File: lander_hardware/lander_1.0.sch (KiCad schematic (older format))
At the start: 26 parts, among them IC1 ATMEGA328-P, J1 Power Connector, P1 Power Supplement, P2 ICSP, P3 XBEE Out, P4 Digital Supplement 1, P5 Digital Supplement 2, P6 Analog Supplement, U1 LD1117S33TR, U2 7805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

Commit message: Simplified continuity tester
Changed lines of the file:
@@
 $EndSheet
 $Comp
-L GND #PWR23
+L GND #PWR22
 U 1 1 58B64C68
 P 11000 3400
-F 0 "#PWR23" H 11000 3150 50  0001 C CNN
+F 0 "#PWR22" H 11000 3150 50  0001 C CNN
 F 1 "GND" H 11000 3250 50  0000 C CNN
 F 2 "" H 11000 3400 50  0000 C CNN
@@
 $EndComp
 $Comp
-L +3.3V #PWR22
+L +3.3V #PWR21
 U 1 1 58B64CE8
 P 11000 2500
-F 0 "#PWR22" H 11000 2350 50  0001 C CNN
+F 0 "#PWR21" H 11000 2350 50  0001 C CNN
 F 1 "+3.3V" H 11000 2640 50  0000 C CNN
 F 2 "" H 11000 2500 50  0000 C CNN
@@
 F6 "Pyro2" I L 9100 4950 60
 F7 "Pyro3" I L 9100 5050 60
-F8 "3.3Vin" I R 10200 4550 60
-F9 "6Vin" I R 10200 4650 60
-F10 "GNDin" I R 10200 4750 60
+F8 "6Vin" I R 10200 4650 60
+F9 "GNDin" I R 10200 4750 60
 $EndSheet
 $Comp
-L +3.3V #PWR19
-U 1 1 58B72CA4
-P 10400 4550
-F 0 "#PWR19" H 10400 4400 50  0001 C CNN
-F 1 "+3.3V" H 10400 4690 50  0000 C CNN
-F 2 "" H 10400 4550 50  0000 C CNN
-F 3 "" H 10400 4550 50  0000 C CNN
-	1    10400 4550
-	1    0    0    -1
-$EndComp
-$Comp
-L +6V #PWR21
+L +6V #PWR20
 U 1 1 58B72D28
 P 10550 4650
-F 0 "#PWR21" H 10550 4500 50  0001 C CNN
+F 0 "#PWR20" H 10550 4500 50  0001 C CNN
 F 1 "+6V" H 10550 4790 50  0000 C CNN
 F 2 "" H 10550 4650 50  0000 C CNN
@@
 $EndComp
 $Comp
-L GND #PWR20
+L GND #PWR19
 U 1 1 58B72DAC
 P 10400 4750
-F 0 "#PWR20" H 10400 4500 50  0001 C CNN
+F 0 "#PWR19" H 10400 4500 50  0001 C CNN
 F 1 "GND" H 10400 4600 50  0000 C CNN
 F 2 "" H 10400 4750 50  0000 C CNN
@@
 	8150 4000 7600 4000
 Wire Wire Line
-	10200 4550 10400 4550
-Wire Wire Line
 	10550 4650 10200 4650

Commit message: Footprints
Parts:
- C1, C2, C3, C4, C5, C6, C7, R2, U2, X1: footprint ~ -> (none)
- IC1: footprint DIL28 -> (none)
- U1: footprint SOT230P700X180-4N -> (none)
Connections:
- net at IC1.13 ((PCINT23/AIN1)PD7): now also U3.2 (IO)
- no-connect marks 0 -> 1
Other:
- moved on the sheet: 100nF1

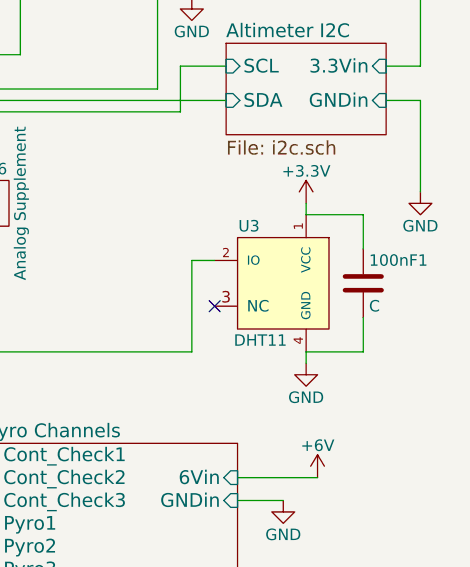
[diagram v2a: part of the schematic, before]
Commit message: Started associating footprints
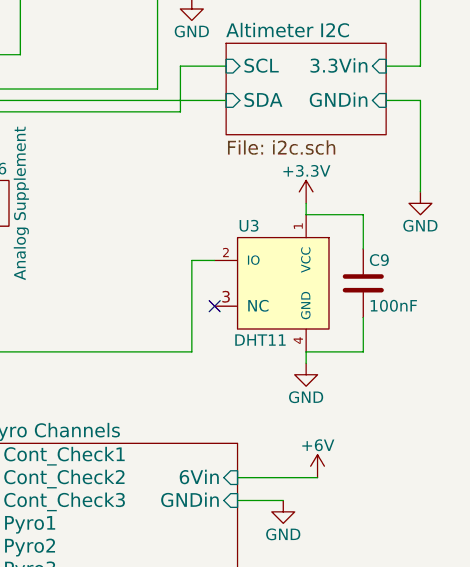
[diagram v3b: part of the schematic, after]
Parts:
- C1: footprint (none) -> Capacitors_THT:C_Disc_D3.0mm_W1.6mm_P2.50mm
- C9: renamed from 100nF1; value C -> 100nF
- IC1: footprint (none) -> Housings_DIP:DIP-28_W7.62mm
- P2: footprint (none) -> Connectors:IDC_Header_Straight_6pins
- R4: footprint (none) -> Opto-Devices:Resistor_LDR_4.9x4.2_RM2.54
- U1: footprint (none) -> footprints:lm1117_nde
- U2: footprint (none) -> Power_Integrations:TO-220
- U3: footprint (none) -> footprints:dht11
- X1: footprint (none) -> Crystals:Crystal_HC49-U_Vertical
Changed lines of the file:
@@
 F 0 "U2" H 3300 1704 60  0000 C CNN
 F 1 "7805" H 3150 2100 60  0000 C CNN
-F 2 "" H 3150 1900 60  0000 C CNN
+F 2 "Power_Integrations:TO-220" H 3150 1900 60  0001 C CNN
 F 3 "~" H 3150 1900 60  0000 C CNN
 	1    3150 1900
@@
 F 0 "U1" H 2250 3050 50  0000 L CNN
 F 1 "LD1117S33TR" H 2150 2450 50  0000 L CNN
-F 2 "" H 2650 2750 50  0001 L CNN
+F 2 "footprints:lm1117_nde" H 2650 2750 50  0001 L CNN
 F 3 "Good" H 2650 2750 50  0001 L CNN
 F 4 "LD1117 Series 1300 mA 3.3 V Fixed Output Positive Voltage LDO Regulator- SOT-223" H 2650 2750 50  0001 L CNN "Description"
@@
 F 0 "C1" H 1700 3400 40  0000 L CNN
 F 1 "10 uF" H 1706 3215 40  0000 L CNN
-F 2 "" H 1738 3150 30  0000 C CNN
+F 2 "Capacitors_THT:C_Disc_D3.0mm_W1.6mm_P2.50mm" H 1738 3150 30  0001 C CNN
 F 3 "~" H 1700 3300 60  0000 C CNN
 	1    1700 3300
@@
 F 0 "C2" H 1950 3400 40  0000 L CNN
 F 1 "10 uF" H 1956 3215 40  0000 L CNN
-F 2 "" H 1988 3150 30  0000 C CNN
+F 2 "" H 1988 3150 30  0001 C CNN
 F 3 "~" H 1950 3300 60  0000 C CNN
 	1    1950 3300
@@
 F 0 "C3" H 3900 3400 40  0000 L CNN
 F 1 "10 uF" H 3906 3215 40  0000 L CNN
-F 2 "" H 3938 3150 30  0000 C CNN
+F 2 "" H 3938 3150 30  0001 C CNN
 F 3 "~" H 3900 3300 60  0000 C CNN
 	1    3900 3300
@@
 F 0 "C4" H 4150 3400 40  0000 L CNN
 F 1 "10 uF" H 4156 3215 40  0000 L CNN
-F 2 "" H 4188 3150 30  0000 C CNN
+F 2 "" H 4188 3150 30  0001 C CNN
 F 3 "~" H 4150 3300 60  0000 C CNN
 	1    4150 3300
@@
 F 0 "IC1" H 5850 4150 40  0000 L BNN
 F 1 "ATMEGA328-P" H 7000 1500 40  0000 L BNN
-F 2 "" H 6600 2900 30  0000 C CIN
+F 2 "Housings_DIP:DIP-28_W7.62mm" H 6600 2900 30  0001 C CIN
 F 3 "" H 6600 2900 60  0000 C CNN
 	1    6600 2900
@@
 F 0 "C5" H 5150 3550 40  0000 L CNN
 F 1 "100 nF" H 5156 3365 40  0000 L CNN
-F 2 "" H 5188 3300 30  0000 C CNN
+F 2 "" H 5188 3300 30  0001 C CNN
 F 3 "~" H 5150 3450 60  0000 C CNN
 	1    5150 3450
@@
 F 0 "X1" H 8350 2600 60  0000 C CNN
 F 1 "16 MHZ" H 8350 2300 60  0000 C CNN
-F 2 "" H 8350 2450 60  0000 C CNN
+F 2 "Crystals:Crystal_HC49-U_Vertical" H 8350 2450 60  0001 C CNN
 F 3 "~" H 8350 2450 60  0000 C CNN
 	1    8350 2450
@@
 F 0 "C6" H 8750 2450 40  0000 L CNN
 F 1 "22 pF" H 8756 2265 40  0000 L CNN
-F 2 "" H 8788 2200 30  0000 C CNN
+F 2 "" H 8788 2200 30  0001 C CNN
 F 3 "~" H 8750 2350 60  0000 C CNN
 	1    8750 2350
@@
 F 0 "C7" H 8750 2700 40  0000 L CNN
 F 1 "22 pF" H 8756 2515 40  0000 L CNN
-F 2 "" H 8788 2450 30  0000 C CNN
+F 2 "" H 8788 2450 30  0001 C CNN
 F 3 "~" H 8750 2600 60  0000 C CNN
 	1    8750 2600
@@
 F 0 "R2" V 6730 1400 40  0000 C CNN
 F 1 "10K" V 6657 1401 40  0000 C CNN
-F 2 "" V 6580 1400 30  0000 C CNN
+F 2 "" V 6580 1400 30  0001 C CNN
 F 3 "~" H 6650 1400 30  0000 C CNN
 	1    6650 1400
@@
 $EndComp
 $Comp
-L C 100nF1
+L C C9
 U 1 1 58B51FA3
 P 10750 3800
-F 0 "100nF1" H 10775 3900 50  0000 L CNN
-F 1 "C" H 10775 3700 50  0000 L CNN
+F 0 "C9" H 10775 3900 50  0000 L CNN
+F 1 "100nF" H 10775 3700 50  0000 L CNN
 F 2 "" H 10788 3650 50  0001 C CNN
 F 3 "" H 10750 3800 50  0000 C CNN
@@
 F 0 "R4" H 9500 2400 50  0000 L CNN
 F 1 "R_PHOTO" H 9500 2350 50  0000 L TNN
-F 2 "" V 9500 2100 50  0001 L CNN
+F 2 "Opto-Devices:Resistor_LDR_4.9x4.2_RM2.54" V 9500 2100 50  0001 L CNN
 F 3 "" H 9450 2300 50  0000 C CNN
 	1    9450 2350
@@
 F 0 "P2" H 8000 1050 50  0000 C CNN
 F 1 "ICSP" H 8000 650 50  0000 C CNN
-F 2 "" H 8000 -350 50  0001 C CNN
+F 2 "Connectors:IDC_Header_Straight_6pins" H 8000 -350 50  0001 C CNN
 F 3 "" H 8000 -350 50  0000 C CNN
 	1    8000 850
@@
 F 0 "U3" H 10550 4050 50  0000 C CNN
 F 1 "DHT11" H 10500 3550 50  0000 C CNN
-F 2 "" H 10550 4050 50  0001 C CNN
+F 2 "footprints:dht11" H 10550 4050 50  0001 C CNN
 F 3 "" H 10550 4050 50  0001 C CNN
 	1    10400 3800

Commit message: Board layout
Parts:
- removed P1: Power Supplement, symbol CONN_01X09
- added P1: Power Out, Pin_Headers:Pin_Header_Straight_1x12_Pitch2.54mm, symbol CONN_01X12
- C1: footprint Capacitors_THT:C_Disc_D3.0mm_W1.6mm_P2.50mm -> Capacitors_THT:C_Disc_D10.0mm_W2.5mm_P5.00mm
- C2, C3, C4, C5, C6, C7, C9: footprint (none) -> Capacitors_THT:C_Disc_D10.0mm_W2.5mm_P5.00mm
- J1: footprint (none) -> Connectors:bornier2
- P3, P6: footprint (none) -> Pin_Headers:Pin_Header_Straight_1x02_Pitch2.54mm
- P4: footprint (none) -> Pin_Headers:Pin_Header_Straight_1x07_Pitch2.54mm
- P5: footprint (none) -> Pin_Headers:Pin_Header_Straight_1x04_Pitch2.54mm
- R1, R2, R3, R5, R6: footprint (none) -> Resistors_THT:R_Axial_DIN0207_L6.3mm_D2.5mm_P10.16mm_Horizontal
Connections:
- net +3V3: now also P1.5 (P5), P1.6 (P6)
- net +5V: now also P1.3 (P3), P1.4 (P4)
- net +6V: now also P1.1 (P1), P1.2 (P2)
- net GND: now also P1.10 (P10), P1.11 (P11), P1.12 (P12), P1.7 (P7), P1.8 (P8), P1.9 (P9)
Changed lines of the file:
@@
 F 0 "C1" H 1700 3400 40  0000 L CNN
 F 1 "10 uF" H 1706 3215 40  0000 L CNN
-F 2 "Capacitors_THT:C_Disc_D3.0mm_W1.6mm_P2.50mm" H 1738 3150 30  0001 C CNN
+F 2 "Capacitors_THT:C_Disc_D10.0mm_W2.5mm_P5.00mm" H 1738 3150 30  0001 C CNN
 F 3 "~" H 1700 3300 60  0000 C CNN
 	1    1700 3300
@@
 F 0 "C2" H 1950 3400 40  0000 L CNN
 F 1 "10 uF" H 1956 3215 40  0000 L CNN
-F 2 "" H 1988 3150 30  0001 C CNN
+F 2 "Capacitors_THT:C_Disc_D10.0mm_W2.5mm_P5.00mm" H 1988 3150 30  0001 C CNN
 F 3 "~" H 1950 3300 60  0000 C CNN
 	1    1950 3300
@@
 F 0 "C3" H 3900 3400 40  0000 L CNN
 F 1 "10 uF" H 3906 3215 40  0000 L CNN
-F 2 "" H 3938 3150 30  0001 C CNN
+F 2 "Capacitors_THT:C_Disc_D10.0mm_W2.5mm_P5.00mm" H 3938 3150 30  0001 C CNN
 F 3 "~" H 3900 3300 60  0000 C CNN
 	1    3900 3300
@@
 F 0 "C4" H 4150 3400 40  0000 L CNN
 F 1 "10 uF" H 4156 3215 40  0000 L CNN
-F 2 "" H 4188 3150 30  0001 C CNN
+F 2 "Capacitors_THT:C_Disc_D10.0mm_W2.5mm_P5.00mm" H 4188 3150 30  0001 C CNN
 F 3 "~" H 4150 3300 60  0000 C CNN
 	1    4150 3300
@@
 F 0 "C5" H 5150 3550 40  0000 L CNN
 F 1 "100 nF" H 5156 3365 40  0000 L CNN
-F 2 "" H 5188 3300 30  0001 C CNN
+F 2 "Capacitors_THT:C_Disc_D10.0mm_W2.5mm_P5.00mm" H 5188 3300 30  0001 C CNN
 F 3 "~" H 5150 3450 60  0000 C CNN
 	1    5150 3450
@@
 F 0 "C6" H 8750 2450 40  0000 L CNN
 F 1 "22 pF" H 8756 2265 40  0000 L CNN
-F 2 "" H 8788 2200 30  0001 C CNN
+F 2 "Capacitors_THT:C_Disc_D10.0mm_W2.5mm_P5.00mm" H 8788 2200 30  0001 C CNN
 F 3 "~" H 8750 2350 60  0000 C CNN
 	1    8750 2350
@@
 F 0 "C7" H 8750 2700 40  0000 L CNN
 F 1 "22 pF" H 8756 2515 40  0000 L CNN
-F 2 "" H 8788 2450 30  0001 C CNN
+F 2 "Capacitors_THT:C_Disc_D10.0mm_W2.5mm_P5.00mm" H 8788 2450 30  0001 C CNN
 F 3 "~" H 8750 2600 60  0000 C CNN
 	1    8750 2600
@@
 F 0 "R2" V 6730 1400 40  0000 C CNN
 F 1 "10K" V 6657 1401 40  0000 C CNN
-F 2 "" V 6580 1400 30  0001 C CNN
+F 2 "Resistors_THT:R_Axial_DIN0207_L6.3mm_D2.5mm_P10.16mm_Horizontal" V 6580 1400 30  0001 C CNN
 F 3 "~" H 6650 1400 30  0000 C CNN
 	1    6650 1400
@@
 F 0 "J1" H 1500 1850 50  0000 C TNN
 F 1 "Power Connector" V 1350 1600 50  0000 C TNN
-F 2 "" H 1500 1375 50  0001 C CNN
+F 2 "Connectors:bornier2" H 1500 1375 50  0001 C CNN
 F 3 "" H 1475 1600 50  0001 C CNN
 	1    1500 1600
@@
 F 0 "C9" H 10775 3900 50  0000 L CNN
 F 1 "100nF" H 10775 3700 50  0000 L CNN
-F 2 "" H 10788 3650 50  0001 C CNN
+F 2 "Capacitors_THT:C_Disc_D10.0mm_W2.5mm_P5.00mm" H 10788 3650 50  0001 C CNN
 F 3 "" H 10750 3800 50  0000 C CNN
 	1    10750 3800
@@
 F 0 "P3" H 8000 1650 50  0000 C CNN
 F 1 "XBEE Out" V 8100 1500 50  0000 C CNN
-F 2 "" H 8000 1500 50  0001 C CNN
+F 2 "Pin_Headers:Pin_Header_Straight_1x02_Pitch2.54mm" H 8000 1500 50  0001 C CNN
 F 3 "" H 8000 1500 50  0000 C CNN
 	1    8000 1500
@@
 F 0 "R6" V 10080 2350 50  0000 C CNN
 F 1 "10K" V 10000 2350 50  0000 C CNN
-F 2 "" V 9930 2350 50  0001 C CNN
+F 2 "Resistors_THT:R_Axial_DIN0207_L6.3mm_D2.5mm_P10.16mm_Horizontal" V 9930 2350 50  0001 C CNN
 F 3 "" H 10000 2350 50  0000 C CNN
 	1    10000 2350
@@
 F 0 "R5" V 10080 1950 50  0000 C CNN
 F 1 "100K" V 10000 1950 50  0000 C CNN
-F 2 "" V 9930 1950 50  0001 C CNN
+F 2 "Resistors_THT:R_Axial_DIN0207_L6.3mm_D2.5mm_P10.16mm_Horizontal" V 9930 1950 50  0001 C CNN
 F 3 "" H 10000 1950 50  0000 C CNN
 	1    10000 1950
@@
 F 0 "R3" V 9530 1950 50  0000 C CNN
 F 1 "47K" V 9450 1950 50  0000 C CNN
-F 2 "" V 9380 1950 50  0001 C CNN
+F 2 "Resistors_THT:R_Axial_DIN0207_L6.3mm_D2.5mm_P10.16mm_Horizontal" V 9380 1950 50  0001 C CNN
 F 3 "" H 9450 1950 50  0000 C CNN
 	1    9450 1950
@@
 F 0 "P5" H 8750 1750 50  0000 C CNN
 F 1 "Digital Supplement 2" V 8850 1500 50  0000 C CNN
-F 2 "" H 8750 1500 50  0001 C CNN
+F 2 "Pin_Headers:Pin_Header_Straight_1x04_Pitch2.54mm" H 8750 1500 50  0001 C CNN
 F 3 "" H 8750 1500 50  0000 C CNN
 	1    8750 1500
@@
 F 0 "P6" H 9150 3600 50  0000 C CNN
 F 1 "Analog Supplement" V 9250 3450 50  0000 C CNN
-F 2 "" H 9150 3450 50  0001 C CNN
+F 2 "Pin_Headers:Pin_Header_Straight_1x02_Pitch2.54mm" H 9150 3450 50  0001 C CNN
 F 3 "" H 9150 3450 50  0000 C CNN
 	1    9150 3450
@@
 F 0 "P4" H 8350 6050 50  0000 C CNN
 F 1 "Digital Supplement 1" V 8450 5650 50  0000 C CNN
-F 2 "" H 8350 5650 50  0001 C CNN
+F 2 "Pin_Headers:Pin_Header_Straight_1x07_Pitch2.54mm" H 8350 5650 50  0001 C CNN
 F 3 "" H 8350 5650 50  0000 C CNN
 	1    8350 5650
@@
 	9950 2850 10150 2850
 $Comp
-L CONN_01X09 P1
-U 1 1 58BC58A9
-P 5800 5700
-F 0 "P1" H 5800 6200 50  0000 C CNN
-F 1 "Power Supplement" V 5900 5700 50  0000 C CNN
-F 2 "" H 5800 5700 50  0001 C CNN
-F 3 "" H 5800 5700 50  0000 C CNN
-	1    5800 5700
-	1    0    0    -1
-$EndComp
-$Comp
 L +5V #PWR018
 U 1 1 58BC59BA
-P 5400 5300
-F 0 "#PWR018" H 5400 5150 50  0001 C CNN
-F 1 "+5V" H 5400 5440 50  0000 C CNN
-F 2 "" H 5400 5300 50  0000 C CNN
-F 3 "" H 5400 5300 50  0000 C CNN
-	1    5400 5300
-	1    0    0    -1
-$EndComp
-Wire Wire Line
-	5400 5300 5600 5300
-Wire Wire Line
-	5600 5400 5500 5400
-Wire Wire Line
-	5500 5300 5500 5500
-Connection ~ 5500 5300
-Wire Wire Line
-	5500 5500 5600 5500
-Connection ~ 5500 5400
+P 5400 5650
+F 0 "#PWR018" H 5400 5500 50  0001 C CNN
+F 1 "+5V" H 5400 5790 50  0000 C CNN
+F 2 "" H 5400 5650 50  0000 C CNN
+F 3 "" H 5400 5650 50  0000 C CNN
+	1    5400 5650
+	1    0    0    -1
+$EndComp
 $Comp
 L +3.3V #PWR019
 U 1 1 58BC5E8A
-P 5400 5700
-F 0 "#PWR019" H 5400 5550 50  0001 C CNN
-F 1 "+3.3V" H 5400 5840 50  0000 C CNN
-F 2 "" H 5400 5700 50  0000 C CNN
-F 3 "" H 5400 5700 50  0000 C CNN
-	1    5400 5700
-	1    0    0    -1
-$EndComp
-Wire Wire Line
-	5400 5700 5600 5700
-Wire Wire Line
-	5500 5600 5500 5800
-Wire Wire Line
-	5500 5800 5600 5800
-Connection ~ 5500 5700
+P 5400 5850
+F 0 "#PWR019" H 5400 5700 50  0001 C CNN
+F 1 "+3.3V" H 5400 5990 50  0000 C CNN
+F 2 "" H 5400 5850 50  0000 C CNN
+F 3 "" H 5400 5850 50  0000 C CNN
+	1    5400 5850
+	1    0    0    -1
+$EndComp
 $Comp
 L GND #PWR020
 U 1 1 58BC636C
-P 5400 6100
-F 0 "#PWR020" H 5400 5850 50  0001 C CNN
-F 1 "GND" H 5400 5950 50  0000 C CNN
-F 2 "" H 5400 6100 50  0000 C CNN
-F 3 "" H 5400 6100 50  0000 C CNN
-	1    5400 6100
-	1    0    0    -1
-$EndComp
-Wire Wire Line
-	5400 6100 5600 6100
-Wire Wire Line
-	5600 6000 5500 6000
-Wire Wire Line
-	5500 5900 5500 6100
-Connection ~ 5500 6100
-Wire Wire Line
-	5600 5900 5500 5900
-Connection ~ 5500 6000
-Wire Wire Line
-	5600 5600 5500 5600
+P 5400 6450
+F 0 "#PWR020" H 5400 6200 50  0001 C CNN
+F 1 "GND" H 5400 6300 50  0000 C CNN
+F 2 "" H 5400 6450 50  0000 C CNN
+F 3 "" H 5400 6450 50  0000 C CNN
+	1    5400 6450
+	1    0    0    -1
+$EndComp
 Wire Wire Line
 	1600 1800 1600 2700
@@
 F 0 "R1" V 5430 2100 50  0000 C CNN
 F 1 "10K" V 5350 2100 50  0000 C CNN
-F 2 "" V 5280 2100 50  0001 C CNN
+F 2 "Resistors_THT:R_Axial_DIN0207_L6.3mm_D2.5mm_P10.16mm_Horizontal" V 5280 2100 50  0001 C CNN
 F 3 "" H 5350 2100 50  0000 C CNN
 	1    5350 2100
@@
 Wire Wire Line
 	10000 3700 10100 3700
+$Comp
+L CONN_01X12 P1
+U 1 1 58BCC7FE
+P 5900 5900
+F 0 "P1" H 5900 6550 50  0000 C CNN
+F 1 "Power Out" V 6000 5900 50  0000 C CNN
+F 2 "Pin_Headers:Pin_Header_Straight_1x12_Pitch2.54mm" H 5900 5900 50  0001 C CNN
+F 3 "" H 5900 5900 50  0000 C CNN
+	1    5900 5900
+	1    0    0    -1
+$EndComp
+Wire Wire Line
+	5700 6450 5400 6450
+Wire Wire Line
+	5550 6350 5700 6350
+Connection ~ 5550 6450
+Wire Wire Line
+	5550 6250 5700 6250
+Connection ~ 5550 6350
+Wire Wire Line
+	5550 6150 5700 6150
+Connection ~ 5550 6250
+Connection ~ 5550 6150
+Wire Wire Line
+	5700 5950 5550 5950
+Wire Wire Line
+	5700 6050 5550 6050
+Wire Wire Line
+	5550 5950 5550 6450
+Connection ~ 5550 6050
+$Comp
+L +6V #PWR025
+U 1 1 58BCD5F7
+P 5400 5450
+F 0 "#PWR025" H 5400 5300 50  0001 C CNN
+F 1 "+6V" H 5400 5590 50  0000 C CNN
+F 2 "" H 5400 5450 50  0000 C CNN
+F 3 "" H 5400 5450 50  0000 C CNN
+	1    5400 5450
+	1    0    0    -1
+$EndComp
+Wire Wire Line
+	5700 5850 5400 5850
+Wire Wire Line
+	5700 5650 5400 5650
+Wire Wire Line
+	5700 5450 5400 5450
+Wire Wire Line
+	5700 5350 5550 5350
+Wire Wire Line
+	5550 5350 5550 5450
+Connection ~ 5550 5450
+Wire Wire Line
+	5700 5550 5550 5550
+Wire Wire Line
+	5550 5550 5550 5650
+Connection ~ 5550 5650
+Wire Wire Line
+	5700 5750 5550 5750
+Wire Wire Line
+	5550 5750 5550 5850
+Connection ~ 5550 5850
 $EndSCHEMATC
